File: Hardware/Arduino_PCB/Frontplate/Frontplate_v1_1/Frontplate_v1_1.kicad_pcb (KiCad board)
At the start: 2 copper layers, 120 x 70 mm, 26 parts, among them J1 Conn_01x03, J2 Conn_01x03, J3 Conn_02x05_Counter_Clockwise, J4 Conn_01x03

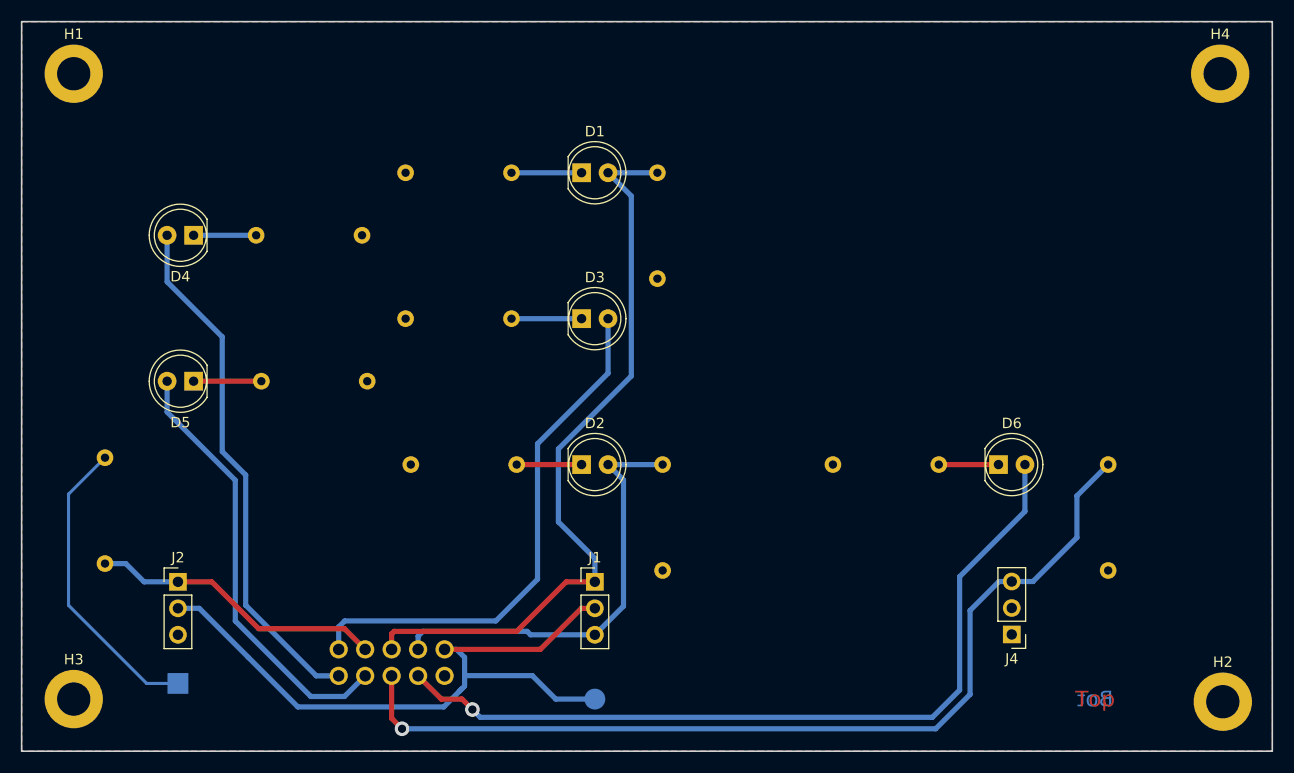
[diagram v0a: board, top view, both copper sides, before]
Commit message: change LED-Connection minor Layout changes
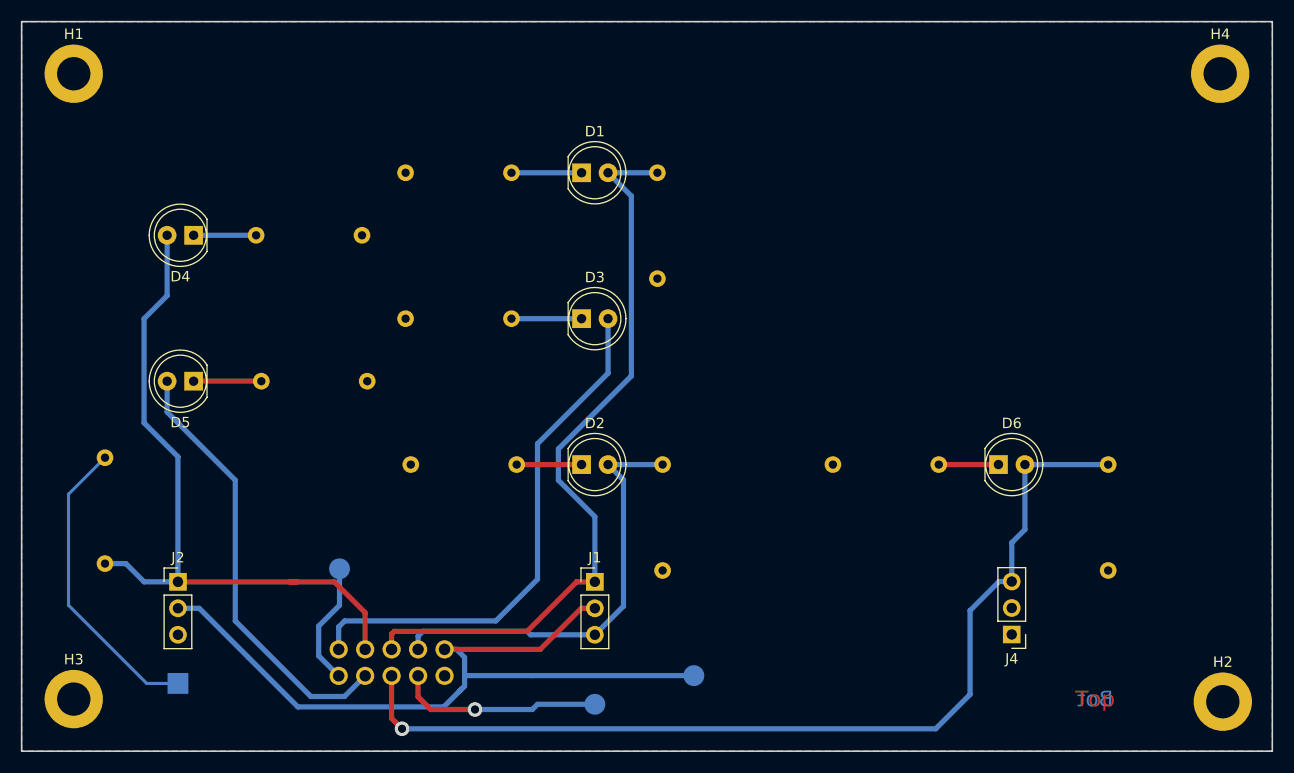
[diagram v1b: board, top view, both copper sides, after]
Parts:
- added TP3: TestPoint, TestPoint:TestPoint_Pad_D2.0mm, B.Cu at (80.5, 132.5)
- added TP4: TestPoint, TestPoint:TestPoint_Pad_D2.0mm, B.Cu at (105.0, 145.5)
- moved TP1 9.76 mm to (114.5, 142.8)
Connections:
- J2 pad 1: Net-(J2-Pad1) -> Net-(D4-Pad2)
- J3 pad 4: Net-(J2-Pad1) -> Net-(D4-Pad2)
- J3 pad 6: Net-(D4-Pad2) -> Net-(J3-Pad6)
- J3 pad 8: Net-(J3-Pad8) -> Net-(D6-Pad2)
- J3 pad 9: Net-(D6-Pad2) -> Net-(J3-Pad9)
- J4 pad 3: Net-(J3-Pad8) -> Net-(D6-Pad2)
- R1 pad 1: Net-(J2-Pad1) -> Net-(D4-Pad2)
- R10 pad 1: Net-(J3-Pad8) -> Net-(D6-Pad2)
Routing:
- net Net-(J3-Pad8): track 90.8 -> 0.00 mm, vias 1 -> 0
- net Net-(J2-Pad1): track 28.4 -> 0.00 mm
- net Net-(J3-Pad9): track 0.00 -> 19.7 mm, vias 0 -> 1
- net Net-(D4-Pad2): track 50.3 -> 66.7 mm
- net Net-(D6-Pad2): track 78.9 -> 94.3 mm
- net Net-(J3-Pad6): track 0.00 -> 11.9 mm
- net +3V3: track 67.1 -> 75.6 mm
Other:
- board text added: "3V3"
- board text added: "Pin 6"
- board text added: "Pin 9"
